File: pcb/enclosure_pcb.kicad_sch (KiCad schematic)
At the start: 8 parts

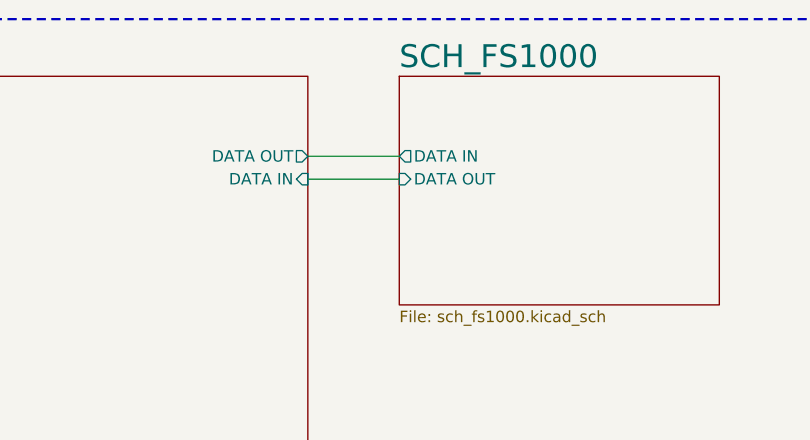
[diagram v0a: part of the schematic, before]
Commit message: feat(layout): component placement
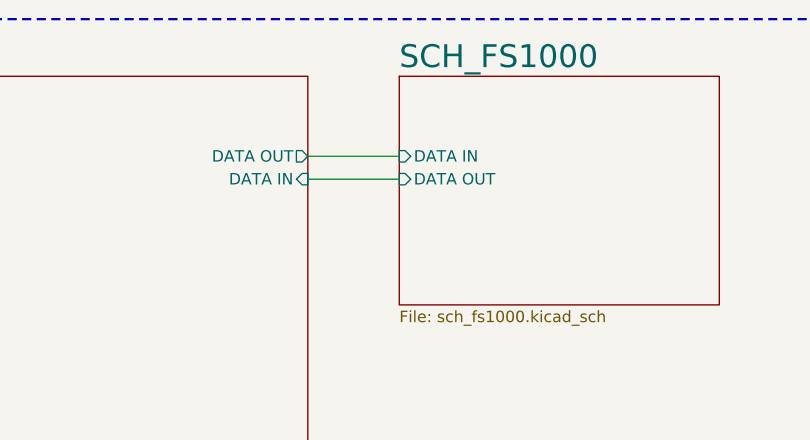
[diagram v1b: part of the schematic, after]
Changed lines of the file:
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@@
 			)
 		)
-		(pin "DATA IN" output
+		(pin "DATA IN" input
 			(at 210.82 35.56 180)
 			(effects
